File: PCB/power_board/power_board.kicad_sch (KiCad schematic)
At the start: 45 parts, among them IC7 BQ51013BRHLR, IC9 MAX17048G+T10, J10 Conn_01x15, J11 Conn_01x15, J7 Conn_01x02, J8 UJ20-C-H-G-MSMT-R-4C-P16-TR, Q2 Si2323DDS-T1-GE3, U2 MCP73871-2CA

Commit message: everything before jlc template
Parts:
- removed J10, J11: Conn_01x15, Connector_PinHeader_2.54mm:PinHeader_1x15_P2.54mm_Vertical, symbol Connector_Generic:Conn_01x15
- added J1: Speaker_con, Connector_PinHeader_2.54mm:PinHeader_1x02_P2.54mm_Vertical, symbol Connector_Generic:Conn_01x02
- added J2: DS1013-40SSIB1-B-0, DS1013-40SSIB1-B-0:DS101340SSIB1B0, symbol DS1013-40SSIB1-B-0:DS1013-40SSIB1-B-0
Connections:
- net BAT+: now also J2.23
- net FG_ALRT: now also J2.17
- net I2C_SCL: now also J2.19
- net I2C_SDA: now also J2.21
- net Movement/ACCEL_CS: now also J2.24
- net Movement/ACCEL_INT1: now also J2.22
- net Movement/ACCEL_INT2: now also J2.20
- net Movement/BCLK: now also J2.18
- net Movement/DATA_IN: now also J2.16
- net Movement/IMU_CS: now also J2.14
- net Movement/IMU_INT1: now also J2.12
- net Movement/IMU_INT2: now also J2.10
- net Movement/MISO: now also J2.8
- net Movement/MOSI: now also J2.6
- net Movement/SCLK: now also J2.4
- net Movement/VOUT_3V3: now also J2.1
- net Movement/WCLK: now also J2.2
- net STAT1: now also J2.13
- net STAT2: now also J2.15
- net STEP_UP/LOUDNESS: now also J2.7
- net STEP_UP/OUT+5V: now also J2.5
- net TS/CTRL: now also J2.3
- net USB_D+: now also J2.9
- net USB_D-: now also J2.11
- new net: J1.1 (Pin_1), J2.27
- new net: J1.2 (Pin_2), J2.25
- no-connect marks 8 -> 16
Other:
- moved on the sheet: C33, IC9, R29, R30, R31

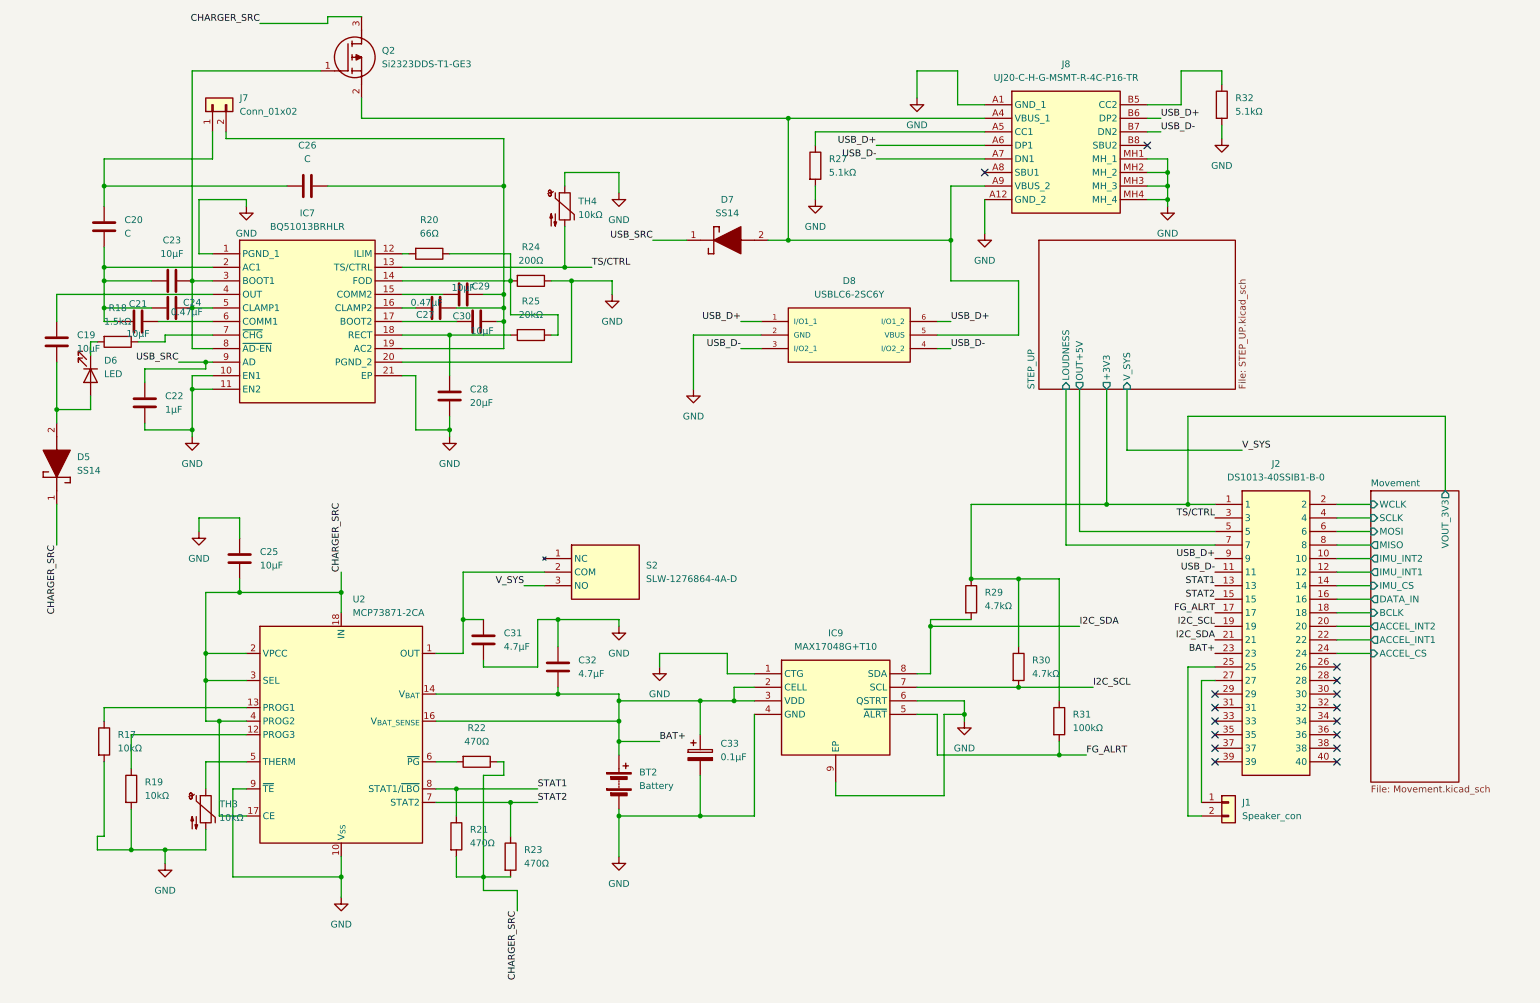
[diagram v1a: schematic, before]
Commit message: verifying schematic and 3V8 power for gsm
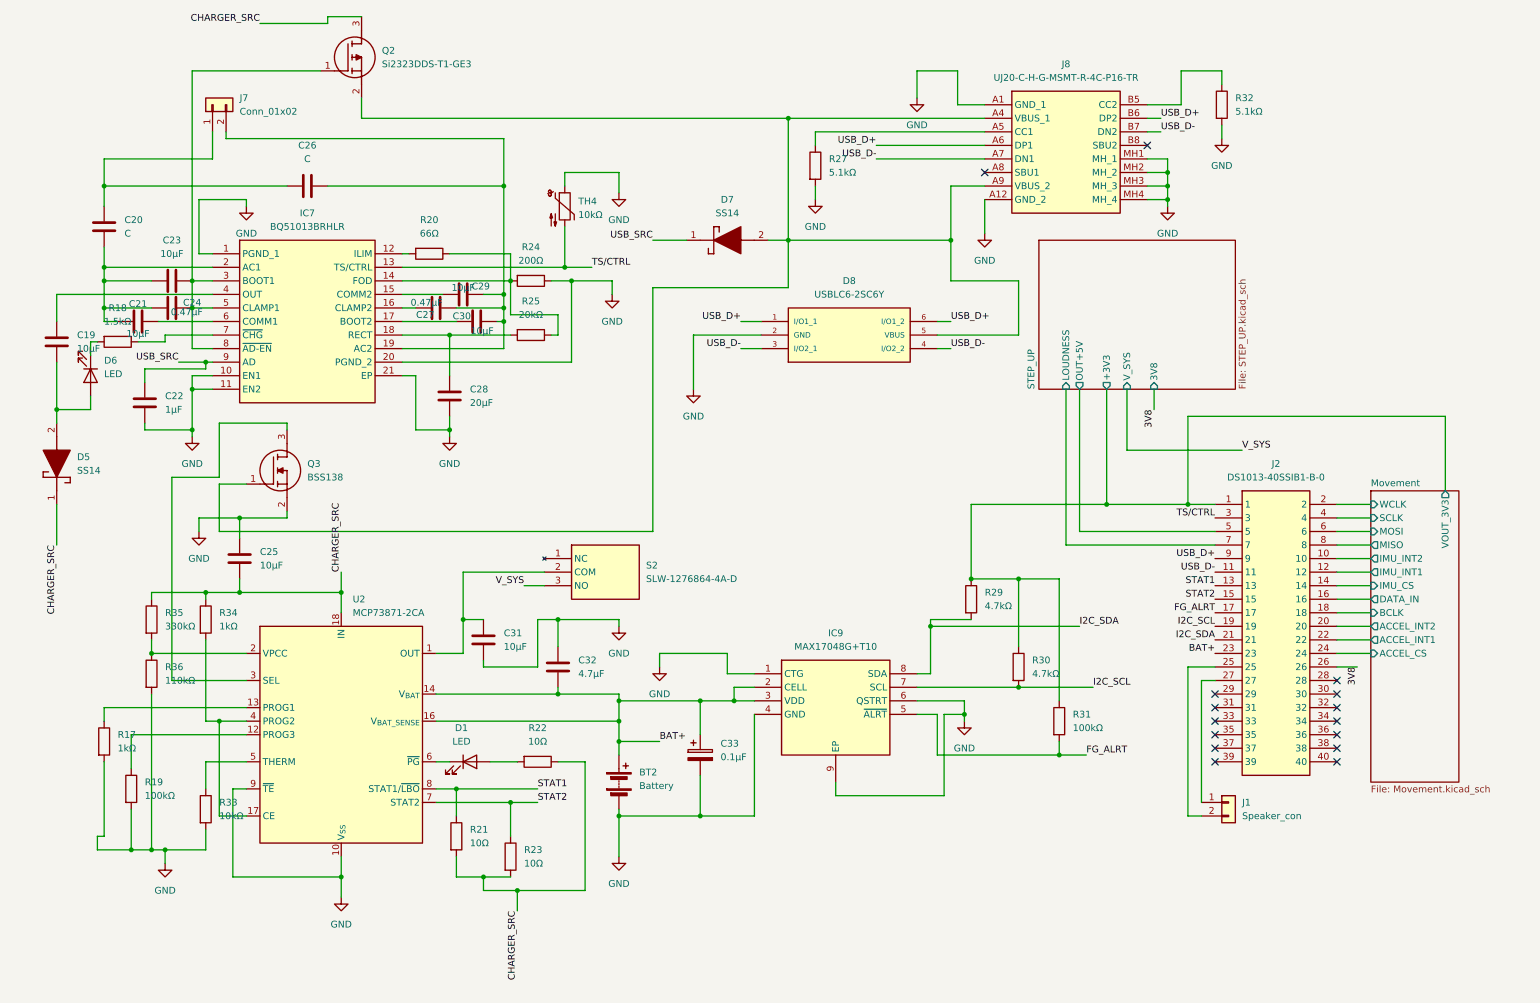
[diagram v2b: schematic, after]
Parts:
- removed TH3: 10kΩ, Resistor_THT:R_Axial_DIN0207_L6.3mm_D2.5mm_P7.62mm_Horizontal, symbol Device:Thermistor_NTC
- added D1: LED, symbol Device:LED
- added Q3: BSS138, SOT95P240X120-3N, symbol BSS138:BSS138
- added R33: 10kΩ, Resistor_THT:R_Axial_DIN0207_L6.3mm_D2.5mm_P7.62mm_Horizontal, symbol Device:R
- added R34: 1kΩ, Resistor_THT:R_Axial_DIN0207_L6.3mm_D2.5mm_P7.62mm_Horizontal, symbol Device:R
- added R35: 330kΩ, Resistor_THT:R_Axial_DIN0207_L6.3mm_D2.5mm_P7.62mm_Horizontal, symbol Device:R
- added R36: 110kΩ, Resistor_THT:R_Axial_DIN0207_L6.3mm_D2.5mm_P7.62mm_Horizontal, symbol Device:R
- C31: value 4.7µF -> 10µF
- R17: value 10kΩ -> 1kΩ
- R19: value 10kΩ -> 100kΩ
- R21, R22, R23: value 470Ω -> 10Ω
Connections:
- net CHARGER_SRC: now also R34.1, R35.1; no longer U2.17 (CE), U2.2 (VPCC), U2.3 (SEL), U2.4 (PROG2)
- net GND: now also Q3.2 (S), R33.2, R36.2
- net at D7.2 (A), D8.5 (VBUS), J8.A4 (VBUS_1)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: now also Q3.1 (G)
- net at U2.5 (THERM): now also R33.1
- net at U2.6 (~{PG}): now also D1.1 (K); no longer R22.2
- net 3V8: now reaches J2.26
- new net: D1.2 (A), R22.2
- new net: R35.2, R36.1, U2.2 (VPCC)
- new net: R34.2, U2.17 (CE), U2.4 (PROG2)
- new net: Q3.3 (D), U2.3 (SEL)
- no-connect marks 16 -> 15
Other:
- sheet STEP_UP ports: added 3V8; removed none
- moved on the sheet: R22

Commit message: induction verified
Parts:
- C20: value C -> C1
- C21, C29: value 10µF -> 22µF
- C26: value C -> C2
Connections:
- net GND: now also C19.2
- net at C20.2, C21.2, C23.2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: now also C26.2
- net at C19.1, IC7.4 (OUT): now also D5.2 (A), D6.2 (A)
- net at C20.1, J7.1 (Pin_1): no longer C26.2
- new net: C23.1, IC7.3 (BOOT1)
- new net: C24.1, IC7.5 (CLAMP1)
- new net: IC7.8 (~{AD-EN}), Q2.1 (G)

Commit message: ECR passed
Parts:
- D1: footprint (none) -> Diode_THT:D_DO-41_SOD81_P7.62mm_Horizontal
- Q3: footprint SOT95P240X120-3N -> BSS138:SOT95P240X120-3N
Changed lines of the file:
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@@
 	)
 	(junction
+		(at 127 172.72)
+		(diameter 0)
+		(color 0 0 0 0)
+	)
+	(junction
 		(at 118.11 64.77)
 		(diameter 0)
@@
 	)
 	(junction
+		(at 64.77 16.51)
+		(diameter 0)
+		(color 0 0 0 0)
+	)
+	(junction
 		(at 229.87 44.45)
 		(diameter 0)
@@
 	(wire
 		(pts
-			(xy 127 151.13) (xy 134.62 151.13)
-		)
-		(stroke
-			(width 0)
-			(type default)
-		)
-	)
-	(wire
-		(pts
 			(xy 44.45 80.01) (xy 49.53 80.01)
 		)
@@
 	(wire
 		(pts
+			(xy 127 151.13) (xy 134.62 151.13)
+		)
+		(stroke
+			(width 0)
+			(type default)
+		)
+	)
+	(wire
+		(pts
 			(xy 226.06 41.91) (xy 229.87 41.91)
 		)
@@
 	(wire
 		(pts
+			(xy 64.77 16.51) (xy 72.39 16.51)
+		)
+		(stroke
+			(width 0)
+			(type default)
+		)
+	)
+	(wire
+		(pts
 			(xy 240.03 35.56) (xy 240.03 38.1)
 		)
@@
 	(wire
 		(pts
+			(xy 64.77 21.59) (xy 64.77 16.51)
+		)
+		(stroke
+			(width 0)
+			(type default)
+		)
+	)
+	(wire
+		(pts
 			(xy 115.57 71.12) (xy 115.57 74.93)
 		)
@@
 	(wire
 		(pts
-			(xy 59.69 16.51) (xy 72.39 16.51)
+			(xy 59.69 16.51) (xy 64.77 16.51)
 		)
 		(stroke
@@
 	(wire
 		(pts
+			(xy 127 172.72) (xy 130.81 172.72)
+		)
+		(stroke
+			(width 0)
+			(type default)
+		)
+	)
+	(wire
+		(pts
 			(xy 52.07 165.1) (xy 52.07 147.32)
 		)
@@
 	(wire
 		(pts
+			(xy 130.81 171.45) (xy 130.81 172.72)
+		)
+		(stroke
+			(width 0)
+			(type default)
+		)
+	)
+	(wire
+		(pts
 			(xy 39.37 123.19) (xy 39.37 124.46)
 		)
@@
 			)
 		)
-		(property "Footprint" ""
+		(property "Footprint" "Diode_THT:D_DO-41_SOD81_P7.62mm_Horizontal"
 			(at 99.06 154.94 0)
 			(hide yes)
@@
 			)
 		)
-		(property "Description" "Low Cap. ESD Protection Auto SOT-23-6 STMicroelectronics USBLC6-2SC6Y, Dual Uni-Directional TVS Diode Array, 6-Pin SOT-23"
+		(property "Description" "17V Clamp 5A (8/20µs) Ipp Tvs Diode Surface Mount SOT-23-6"
 			(at 153.67 72.39 0)
 			(hide yes)
@@
 	)
 	(symbol
+		(lib_id "power:PWR_FLAG")
+		(at 130.81 171.45 0)
+		(unit 1)
+		(body_style 1)
+		(exclude_from_sim no)
+		(in_bom yes)
+		(on_board yes)
+		(in_pos_files yes)
+		(dnp no)
+		(fields_autoplaced yes)
+		(property "Reference" "#FLG02"
+			(at 130.81 169.545 0)
+			(hide yes)
+			(show_name no)
+			(do_not_autoplace no)
+			(effects
+				(font
+					(size 1.27 1.27)
+				)
+			)
+		)
+		(property "Value" "PWR_FLAG"
+			(at 130.81 166.37 0)
+			(show_name no)
+			(do_not_autoplace no)
+			(effects
+				(font
+					(size 1.27 1.27)
+				)
+			)
+		)
+		(property "Footprint" ""
+			(at 130.81 171.45 0)
+			(hide yes)
+			(show_name no)
+			(do_not_autoplace no)
+			(effects
+				(font
+					(size 1.27 1.27)
+				)
+			)
+		)
+		(property "Datasheet" ""
+			(at 130.81 171.45 0)
+			(hide yes)
+			(show_name no)
+			(do_not_autoplace no)
+			(effects
+				(font
+					(size 1.27 1.27)
+				)
+			)
+		)
+		(property "Description" "Special symbol for telling ERC where power comes from"
+			(at 130.81 171.45 0)
+			(hide yes)
+			(show_name no)
+			(do_not_autoplace no)
+			(effects
+				(font
+					(size 1.27 1.27)
+				)
+			)
+		)
+		(pin "1"
+		)
+		(instances
+			(project "power_board"
+				(path "/f044e945-eb74-49fa-825d-5f99d2d7b949"
+					(reference "#FLG02")
+					(unit 1)
+				)
+			)
+		)
+	)
+	(symbol
 		(lib_id "power:GND")
 		(at 182.88 30.48 0)
@@
 	)
 	(symbol
+		(lib_id "power:PWR_FLAG")
+		(at 64.77 21.59 180)
+		(unit 1)
+		(body_style 1)
+		(exclude_from_sim no)
+		(in_bom yes)
+		(on_board yes)
+		(in_pos_files yes)
+		(dnp no)
+		(fields_autoplaced yes)
+		(property "Reference" "#FLG03"
+			(at 64.77 23.495 0)
+			(hide yes)
+			(show_name no)
+			(do_not_autoplace no)
+			(effects
+				(font
+					(size 1.27 1.27)
+				)
+			)
+		)
+		(property "Value" "PWR_FLAG"
+			(at 64.77 26.67 0)
+			(show_name no)
+			(do_not_autoplace no)
+			(effects
+				(font
+					(size 1.27 1.27)
+				)
+			)
+		)
+		(property "Footprint" ""
+			(at 64.77 21.59 0)
+			(hide yes)
+			(show_name no)
+			(do_not_autoplace no)
+			(effects
+				(font
+					(size 1.27 1.27)
+				)
+			)
+		)
+		(property "Datasheet" ""
+			(at 64.77 21.59 0)
+			(hide yes)
+			(show_name no)
+			(do_not_autoplace no)
+			(effects
+				(font
+					(size 1.27 1.27)
+				)
+			)
+		)
+		(property "Description" "Special symbol for telling ERC where power comes from"
+			(at 64.77 21.59 0)
+			(hide yes)
+			(show_name no)
+			(do_not_autoplace no)
+			(effects
+				(font
+					(size 1.27 1.27)
+				)
+			)
+		)
+		(pin "1"
+		)
+		(instances
+			(project "power_board"
+				(path "/f044e945-eb74-49fa-825d-5f99d2d7b949"
+					(reference "#FLG03")
+					(unit 1)
+				)
+			)
+		)
+	)
+	(symbol
 		(lib_id "power:GND")
 		(at 41.91 173.99 0)
@@
 			)
 		)
-		(property "Footprint" "SOT95P240X120-3N"
+		(property "Footprint" "BSS138:SOT95P240X120-3N"
 			(at 68.58 201.6 0)
 			(hide yes)

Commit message: two layers routing done
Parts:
- renumbered J7 to indukcja1
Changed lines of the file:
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@@
 		(dnp no)
 		(fields_autoplaced yes)
-		(property "Reference" "J7"
+		(property "Reference" "indukcja1"
 			(at 55.88 30.4799 90)
 			(show_name no)
@@
 			(project "power_board"
 				(path "/f044e945-eb74-49fa-825d-5f99d2d7b949"
-					(reference "J7")
+					(reference "indukcja1")
 					(unit 1)
 				)

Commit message: own routes with errors done
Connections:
- net 3V8: now also J2.2; no longer J2.26
- net Movement/ACCEL_INT1: now also J2.20; no longer J2.22
- net Movement/ACCEL_INT2: now also J2.22; no longer J2.20
- net Movement/MISO: now also J2.6; no longer J2.8
- net Movement/MOSI: now also J2.8; no longer J2.6
- net Movement/WCLK: now also J2.26; no longer J2.2
- net USB_D+: now also J2.37; no longer J2.9
- net USB_D-: now also J2.39; no longer J2.11
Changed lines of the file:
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@@
 	)
 	(no_connect
-		(at 238.76 154.94)
+		(at 238.76 119.38)
+	)
+	(no_connect
+		(at 238.76 116.84)
 	)
 	(no_connect
@@
 	)
 	(no_connect
-		(at 238.76 152.4)
-	)
-	(no_connect
 		(at 261.62 147.32)
 	)
@@
 	(wire
 		(pts
+			(xy 266.7 129.54) (xy 266.7 130.81)
+		)
+		(stroke
+			(width 0)
+			(type default)
+		)
+	)
+	(wire
+		(pts
 			(xy 226.06 36.83) (xy 228.6 36.83)
 		)
@@
 	(wire
 		(pts
-			(xy 261.62 132.08) (xy 267.97 132.08)
+			(xy 267.97 129.54) (xy 266.7 129.54)
+		)
+		(stroke
+			(width 0)
+			(type default)
+		)
+	)
+	(wire
+		(pts
+			(xy 265.43 114.3) (xy 265.43 113.03)
+		)
+		(stroke
+			(width 0)
+			(type default)
+		)
+	)
+	(wire
+		(pts
+			(xy 266.7 106.68) (xy 266.7 99.06)
 		)
 		(stroke
@@
 	(wire
 		(pts
+			(xy 261.62 114.3) (xy 264.16 114.3)
+		)
+		(stroke
+			(width 0)
+			(type default)
+		)
+	)
+	(wire
+		(pts
+			(xy 264.16 132.08) (xy 261.62 132.08)
+		)
+		(stroke
+			(width 0)
+			(type default)
+		)
+	)
+	(wire
+		(pts
 			(xy 54.61 160.02) (xy 54.61 176.53)
 		)
@@
 	(wire
 		(pts
+			(xy 278.13 99.06) (xy 278.13 137.16)
+		)
+		(stroke
+			(width 0)
+			(type default)
+		)
+	)
+	(wire
+		(pts
 			(xy 191.77 143.51) (xy 191.77 146.05)
 		)
@@
 	(wire
 		(pts
+			(xy 278.13 137.16) (xy 261.62 137.16)
+		)
+		(stroke
+			(width 0)
+			(type default)
+		)
+	)
+	(wire
+		(pts
 			(xy 133.35 66.04) (xy 133.35 111.76)
 		)
@@
 	(wire
 		(pts
+			(xy 231.14 156.21) (xy 238.76 156.21)
+		)
+		(stroke
+			(width 0)
+			(type default)
+		)
+	)
+	(wire
+		(pts
 			(xy 186.69 72.39) (xy 189.23 72.39)
 		)
@@
 	(wire
 		(pts
+			(xy 267.97 132.08) (xy 265.43 132.08)
+		)
+		(stroke
+			(width 0)
+			(type default)
+		)
+	)
+	(wire
+		(pts
 			(xy 261.62 116.84) (xy 267.97 116.84)
 		)
@@
 	(wire
 		(pts
+			(xy 266.7 130.81) (xy 264.16 130.81)
+		)
+		(stroke
+			(width 0)
+			(type default)
+		)
+	)
+	(wire
+		(pts
 			(xy 218.44 106.68) (xy 233.68 106.68)
 		)
@@
 	(wire
 		(pts
+			(xy 267.97 114.3) (xy 265.43 114.3)
+		)
+		(stroke
+			(width 0)
+			(type default)
+		)
+	)
+	(wire
+		(pts
 			(xy 227.33 85.09) (xy 227.33 88.9)
 		)
@@
 	(wire
 		(pts
+			(xy 238.76 156.21) (xy 238.76 154.94)
+		)
+		(stroke
+			(width 0)
+			(type default)
+		)
+	)
+	(wire
+		(pts
 			(xy 233.68 137.16) (xy 233.68 165.1)
 		)
@@
 	(wire
 		(pts
+			(xy 267.97 111.76) (xy 264.16 111.76)
+		)
+		(stroke
+			(width 0)
+			(type default)
+		)
+	)
+	(wire
+		(pts
 			(xy 52.07 101.6) (xy 43.18 101.6)
 		)
@@
 	(wire
 		(pts
+			(xy 232.41 152.4) (xy 238.76 152.4)
+		)
+		(stroke
+			(width 0)
+			(type default)
+		)
+	)
+	(wire
+		(pts
 			(xy 46.99 82.55) (xy 46.99 85.09)
 		)
@@
 	(wire
 		(pts
+			(xy 266.7 99.06) (xy 278.13 99.06)
+		)
+		(stroke
+			(width 0)
+			(type default)
+		)
+	)
+	(wire
+		(pts
 			(xy 189.23 64.77) (xy 189.23 57.15)
 		)
@@
 	(wire
 		(pts
+			(xy 265.43 129.54) (xy 261.62 129.54)
+		)
+		(stroke
+			(width 0)
+			(type default)
+		)
+	)
+	(wire
+		(pts
 			(xy 49.53 154.94) (xy 49.53 160.02)
 		)
@@
 	(wire
 		(pts
+			(xy 264.16 106.68) (xy 261.62 106.68)
+		)
+		(stroke
+			(width 0)
+			(type default)
+		)
+	)
+	(wire
+		(pts
 			(xy 152.4 138.43) (xy 147.32 138.43)
 		)
@@
 	(wire
 		(pts
+			(xy 264.16 104.14) (xy 264.16 106.68)
+		)
+		(stroke
+			(width 0)
+			(type default)
+		)
+	)
+	(wire
+		(pts
 			(xy 57.15 160.02) (xy 54.61 160.02)
 		)
@@
 	(wire
 		(pts
-			(xy 261.62 106.68) (xy 267.97 106.68)
+			(xy 125.73 64.77) (xy 125.73 67.31)
 		)
 		(stroke
@@
 	(wire
 		(pts
-			(xy 125.73 64.77) (xy 125.73 67.31)
+			(xy 267.97 106.68) (xy 266.7 106.68)
 		)
 		(stroke
@@
 	(wire
 		(pts
+			(xy 264.16 111.76) (xy 264.16 114.3)
+		)
+		(stroke
+			(width 0)
+			(type default)
+		)
+	)
+	(wire
+		(pts
 			(xy 226.06 41.91) (xy 229.87 41.91)
 		)
@@
 	(wire
 		(pts
+			(xy 262.89 111.76) (xy 261.62 111.76)
+		)
+		(stroke
+			(width 0)
+			(type default)
+		)
+	)
+	(wire
+		(pts
 			(xy 281.94 90.17) (xy 281.94 104.14)
 		)
@@
 	(wire
 		(pts
+			(xy 265.43 113.03) (xy 262.89 113.03)
+		)
+		(stroke
+			(width 0)
+			(type default)
+		)
+	)
+	(wire
+		(pts
 			(xy 127 165.1) (xy 142.24 165.1)
 		)
@@
 	(wire
 		(pts
+			(xy 264.16 130.81) (xy 264.16 132.08)
+		)
+		(stroke
+			(width 0)
+			(type default)
+		)
+	)
+	(wire
+		(pts
 			(xy 142.24 143.51) (xy 142.24 149.86)
 		)
@@
 	(wire
 		(pts
-			(xy 261.62 137.16) (xy 265.43 137.16)
+			(xy 20.32 57.15) (xy 20.32 54.61)
 		)
 		(stroke
@@
 	(wire
 		(pts
-			(xy 20.32 57.15) (xy 20.32 54.61)
+			(xy 105.41 46.99) (xy 72.39 46.99)
 		)
 		(stroke
@@
 	(wire
 		(pts
-			(xy 105.41 46.99) (xy 72.39 46.99)
+			(xy 262.89 113.03) (xy 262.89 111.76)
 		)
 		(stroke
@@
 	(wire
 		(pts
-			(xy 261.62 111.76) (xy 267.97 111.76)
-		)
-		(stroke
-			(width 0)
-			(type default)
-		)
-	)
-	(wire
-		(pts
 			(xy 152.4 143.51) (xy 148.59 143.51)
 		)
@@
 	(wire
 		(pts
-			(xy 261.62 114.3) (xy 267.97 114.3)
-		)
-		(stroke
-			(width 0)
-			(type default)
-		)
-	)
-	(wire
-		(pts
 			(xy 64.77 91.44) (xy 52.07 91.44)
 		)
@@
 	(wire
 		(pts
+			(xy 265.43 132.08) (xy 265.43 129.54)
+		)
+		(stroke
+			(width 0)
+			(type default)
+		)
+	)
+	(wire
+		(pts
 			(xy 127 48.26) (xy 127 44.45)
 		)
@@
 	(wire
 		(pts
-			(xy 261.62 129.54) (xy 267.97 129.54)
-		)
-		(stroke
-			(width 0)
-			(type default)
-		)
-	)
-	(wire
-		(pts
 			(xy 115.57 128.27) (xy 127 128.27)
 		)
@@
 	)
 	(label "3V8"
-		(at 265.43 137.16 270)
+		(at 264.16 104.14 90)
 		(effects
 			(font
 				(size 1.27 1.27)
 			)
-			(justify right bottom)
+			(justify left bottom)
 		)
 	)
@@
 		)
 	)
-	(label "CHARGER_SRC"
-		(at 74.93 119.38 90)
+	(label "USB_D-"
+		(at 231.14 156.21 180)
 		(effects
 			(font
 				(size 1.27 1.27)
 			)
-			(justify left bottom)
+			(justify right bottom)
 		)
 	)
-	(label "BAT+"
-		(at 238.76 134.62 180)
+	(label "CHARGER_SRC"
+		(at 74.93 119.38 90)
 		(effects
 			(font
 				(size 1.27 1.27)
 			)
-			(justify right bottom)
+			(justify left bottom)
 		)
 	)
-	(label "USB_D-"
-		(at 238.76 119.38 180)
+	(label "BAT+"
+		(at 238.76 134.62 180)
 		(effects
 			(font
@@
 	)
 	(label "USB_D+"
-		(at 238.76 116.84 180)
+		(at 232.41 152.4 180)
 		(effects
 			(font

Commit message: everything checked
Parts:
- added H1, H2, H3, H4: MountingHole, MountingHole:MountingHole_3.2mm_M3_Pad_Via, symbol Mechanical:MountingHole
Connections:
- net GND: now also J2.40
- net USB_D+: no longer D8.6 (I/O1_2), J2.37
- net USB_D-: no longer D8.4 (I/O2_2), J2.39
- new net USB_D+_S: D8.6 (I/O1_2), J2.37
- new net USB_D-_S: D8.4 (I/O2_2), J2.39
- no-connect marks 15 -> 14

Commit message: all my pcb
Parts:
- removed J8: UJ20-C-H-G-MSMT-R-4C-P16-TR, UJ20-C-H-G-MSMT-R-4C-P16-TR:UJ20CHGMSMTR4CP16TR, symbol UJ20-C-H-G-MSMT-R-4C-P16-TR:UJ20-C-H-G-MSMT-R-4C-P16-TR
- added J3: USB4110GFA, USB4110GFA:GCT_USB4110GFA, symbol USB4110GFA:USB4110GFA
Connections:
- net GND: now also J3.A1/B12 (GND), J3.B1/A12 (GND), J3.S1 (GND), J3.S2 (GND), J3.S3 (GND), J3.S4 (GND)
- net USB_D+: now also J3.A6 (DP1), J3.B6 (DP2)
- net USB_D-: now also J3.A7 (DN1), J3.B7 (DN2)
- net VBUS: now reaches D7.2 (A), D8.5 (VBUS), Q2.2 (S), Q3.1 (G)
- net VBUS: now also J3.A4/B9 (VBUS), J3.B4/A9 (VBUS)
- net at R27.1: now also J3.A5 (CC1)
- net at R32.1: now also J3.B5 (CC2)
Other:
- moved on the sheet: R32
